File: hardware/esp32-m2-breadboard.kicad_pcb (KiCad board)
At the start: 2 copper layers, 57.2 x 22.9 mm, 4 parts, among them J1 2199230-4, J2 Conn_01x16_Female, J3 Conn_01x16_Female

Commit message: Pins assigned
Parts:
- J2, J3: value Conn_01x16_Female -> Conn_01x15_Female; footprint Connector_PinHeader_2.54mm:PinHeader_1x16_P2.54mm_Vertical -> Connector_PinHeader_2.54mm:PinHeader_1x15_P2.54mm_Vertical
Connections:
- J1 pad 1: Net-(J1-Pad1) -> GND
- J1 pad 10: Net-(J1-Pad10) -> /GPIO19
- J1 pad 11: Net-(J1-Pad11) -> /GPIO15
- J1 pad 12: Net-(J1-Pad12) -> /GPIO23
- J1 pad 13: Net-(J1-Pad13) -> /GPIO2
- J1 pad 14: Net-(J1-Pad14) -> /GPIO5
- J1 pad 15: Net-(J1-Pad15) -> /GPIO4
- J1 pad 18: Net-(J1-Pad18) -> GND
- J1 pad 19: Net-(J1-Pad19) -> /GPIO16
- J1 pad 22: Net-(J1-Pad22) -> /TX
- J1 pad 32: Net-(J1-Pad32) -> /RX
- J1 pad 33: Net-(J1-Pad33) -> GND
- J1 pad 34: Net-(J1-Pad34) -> /RTS
- J1 pad 36: Net-(J1-Pad36) -> /DTR
- J1 pad 39: Net-(J1-Pad39) -> GND
- J1 pad 41: Net-(J1-Pad41) -> /GPIO22
- J1 pad 43: Net-(J1-Pad43) -> /GPIO21
- J1 pad 45: Net-(J1-Pad45) -> GND
- J1 pad 50: Net-(J1-Pad50) -> /RESET
- J1 pad 51: Net-(J1-Pad51) -> GND
- J1 pad 57: Net-(J1-Pad57) -> GND
- J1 pad 58: Net-(J1-Pad58) -> /GPIO32
- J1 pad 59: Net-(J1-Pad59) -> /GPIO27
- J1 pad 60: Net-(J1-Pad60) -> /GPIO33
- J1 pad 61: Net-(J1-Pad61) -> /GPIO26-DAC2
- J1 pad 63: Net-(J1-Pad63) -> GND
- J1 pad 64: Net-(J1-Pad64) -> /GPIO25-DAC1
- J1 pad 69: Net-(J1-Pad69) -> GND
- J1 pad 7: Net-(J1-Pad7) -> GND
- J1 pad 72: Net-(J1-Pad72) -> +5V
- J1 pad 74: Net-(J1-Pad74) -> +5V
- J1 pad 75: Net-(J1-Pad75) -> GND
- J1 pad 8: Net-(J1-Pad8) -> /GPIO18
- J1 pad S1: Net-(J1-PadS1) -> GND
- J1 pad S2: Net-(J1-PadS1) -> GND
- J2 pad 1: Net-(J2-Pad1) -> +5V
- J2 pad 10: Net-(J2-Pad10) -> /GPIO21
- J2 pad 11: Net-(J2-Pad11) -> /GPIO22
- J2 pad 12: Net-(J2-Pad12) -> GND
- J2 pad 13: Net-(J2-Pad13) -> GND
- J2 pad 14: Net-(J2-Pad14) -> GND
- J2 pad 15: Net-(J2-Pad15) -> GND
- J2 pad 2: Net-(J2-Pad2) -> +5V
- J2 pad 3: Net-(J2-Pad3) -> GND
- J2 pad 4: Net-(J2-Pad4) -> /GPIO25-DAC1
- J2 pad 5: Net-(J2-Pad5) -> /GPIO26-DAC2
- J2 pad 6: Net-(J2-Pad6) -> /GPIO33
- J2 pad 7: Net-(J2-Pad7) -> /GPIO27
- J2 pad 8: Net-(J2-Pad8) -> /GPIO32
- J2 pad 9: Net-(J2-Pad9) -> /RESET
- J3 pad 1: Net-(J3-Pad1) -> GND
- J3 pad 10: Net-(J3-Pad10) -> /GPIO4
- J3 pad 11: Net-(J3-Pad11) -> /GPIO16
- J3 pad 12: Net-(J3-Pad12) -> /TX
- J3 pad 13: Net-(J3-Pad13) -> /RX
- J3 pad 14: Net-(J3-Pad14) -> /RTS
- J3 pad 15: Net-(J3-Pad15) -> /DTR
- J3 pad 2: Net-(J3-Pad2) -> GND
- J3 pad 3: Net-(J3-Pad3) -> GND
- J3 pad 4: Net-(J3-Pad4) -> /GPIO18
- J3 pad 5: Net-(J3-Pad5) -> /GPIO19
- J3 pad 6: Net-(J3-Pad6) -> /GPIO15
- J3 pad 7: Net-(J3-Pad7) -> /GPIO23
- J3 pad 8: Net-(J3-Pad8) -> /GPIO2
- J3 pad 9: Net-(J3-Pad9) -> /GPIO5
- MP1 pad 1: Net-(MP1-Pad1) -> GND
- MP1 pad 2: Net-(MP1-Pad1) -> GND
- MP1 pad 3: Net-(MP1-Pad1) -> GND
- MP1 pad 4: Net-(MP1-Pad1) -> GND
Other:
- outline, holes or cut-outs redrawn

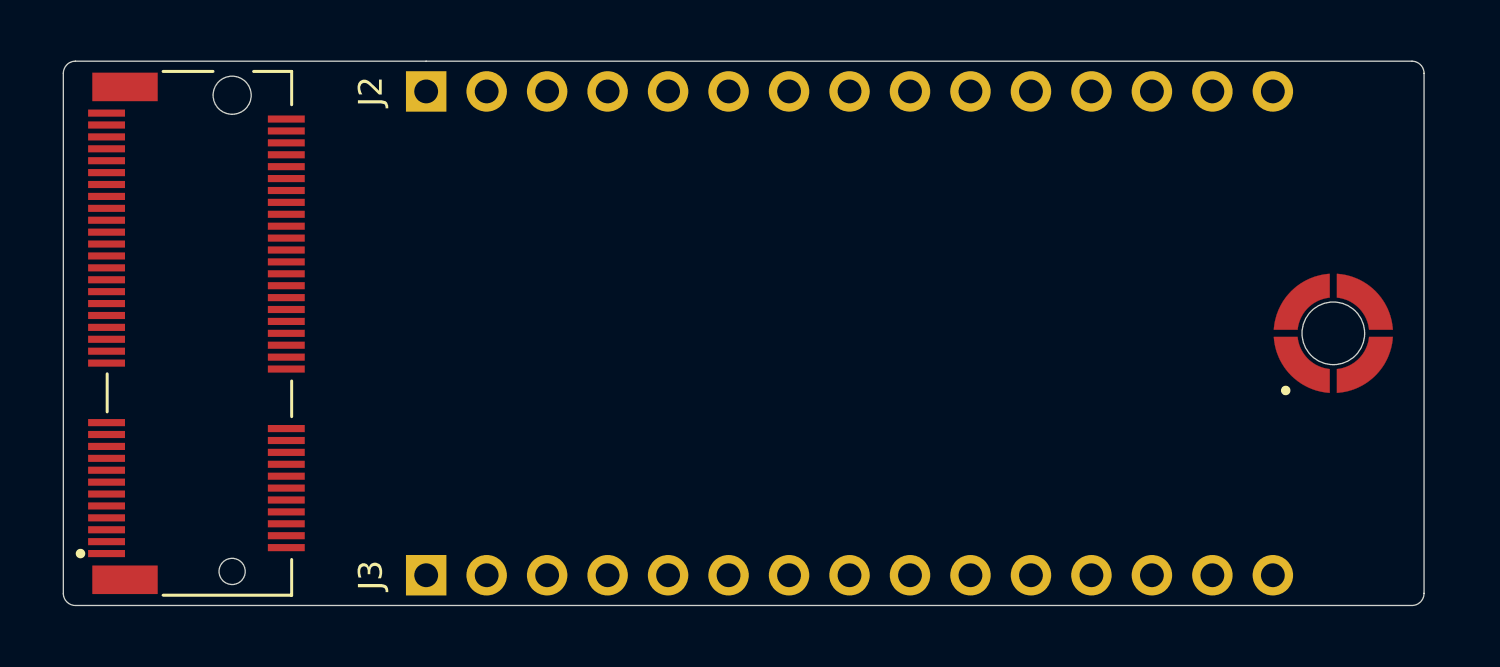
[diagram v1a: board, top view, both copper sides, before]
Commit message: First routing done
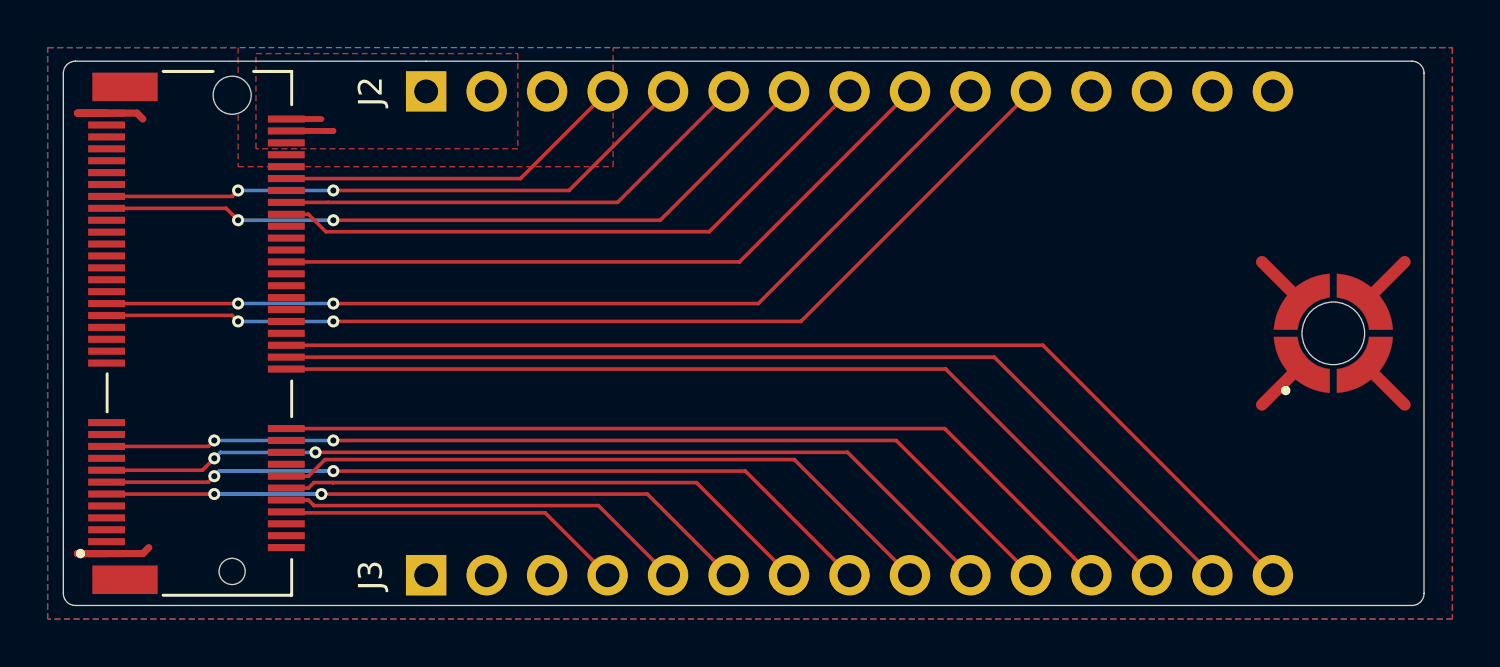
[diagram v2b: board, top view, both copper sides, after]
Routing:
- net /DTR: track 0.00 -> 45.4 mm
- net /GPIO22: track 0.00 -> 42.9 mm, vias 0 -> 2
- net /RTS: track 0.00 -> 42.7 mm
- net /GPIO16: track 0.00 -> 41.3 mm, vias 0 -> 2
- net /GPIO21: track 0.00 -> 40.0 mm, vias 0 -> 2
- net /RX: track 0.00 -> 39.9 mm
- net /GPIO4: track 0.00 -> 38.7 mm, vias 0 -> 2
- net /TX: track 0.00 -> 36.4 mm
- net /GPIO2: track 0.00 -> 33.2 mm, vias 0 -> 2
- net /GPIO27: track 0.00 -> 31.1 mm, vias 0 -> 2
- net /RESET: track 0.00 -> 29.2 mm
- net /GPIO5: track 0.00 -> 28.5 mm
- net /GPIO15: track 0.00 -> 27.5 mm, vias 0 -> 2
- net /GPIO32: track 0.00 -> 26.4 mm
- net /GPIO26-DAC2: track 0.00 -> 25.4 mm, vias 0 -> 2
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- added copper zone on F.Cu, net +5V
- added copper zone on B.Cu, net GND
- added copper zone on F.Cu, net GND
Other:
- net class Default: clearance 0.2 -> 0.1524
- rule trace_clearance: 0.2 -> 0.1524
- rule trace_min: 0.2 -> 0.1524
- rule via_min_drill: 0.3 -> 0.254

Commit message: Add name,date,rev on silkscreen
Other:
- board text added: "François Gervais 19 jan 2021 Rev 1.0"
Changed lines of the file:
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@@
   (general
     (thickness 1.6)
-    (drawings 9)
+    (drawings 10)
     (tracks 108)
     (zones 0)
@@
     )
   )
+  (gr_text "François Gervais\n19 jan 2021\nRev 1.0" (at 85.5 94.5) (layer F.SilkS)
+    (effects (font (size 1 1) (thickness 0.15)) (justify left))
+  )
   (gr_arc (start 47.168 110.922) (end 46.66 110.922) (angle -90) (layer Edge.Cuts) (width 0.05))
